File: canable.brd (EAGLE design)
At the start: 19.1 x 45.1 mm, 25 parts, among them J2 USB-MICROB, U2 AP2202K-3.3TRG1, U3 MCP2551

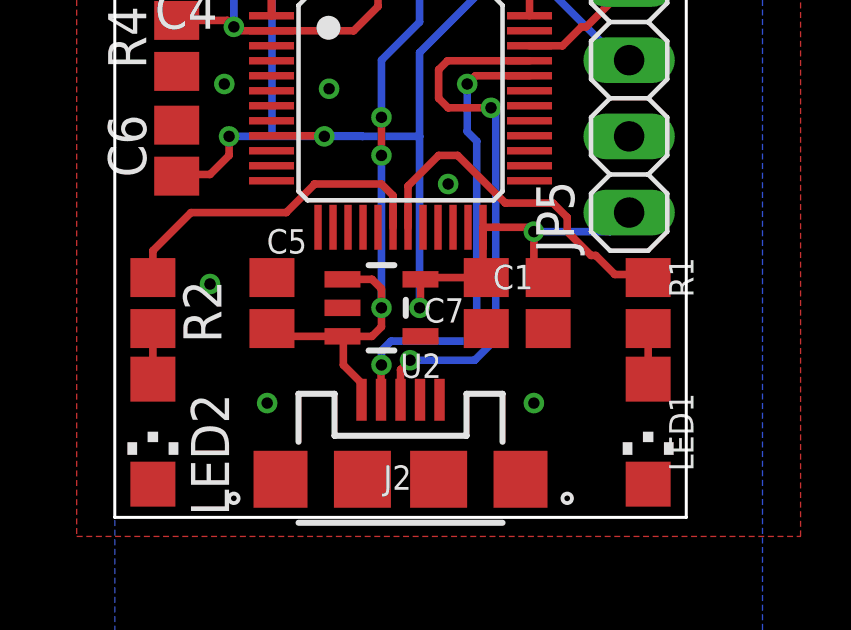
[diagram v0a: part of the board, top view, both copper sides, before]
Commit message: bom changed and screw holes added
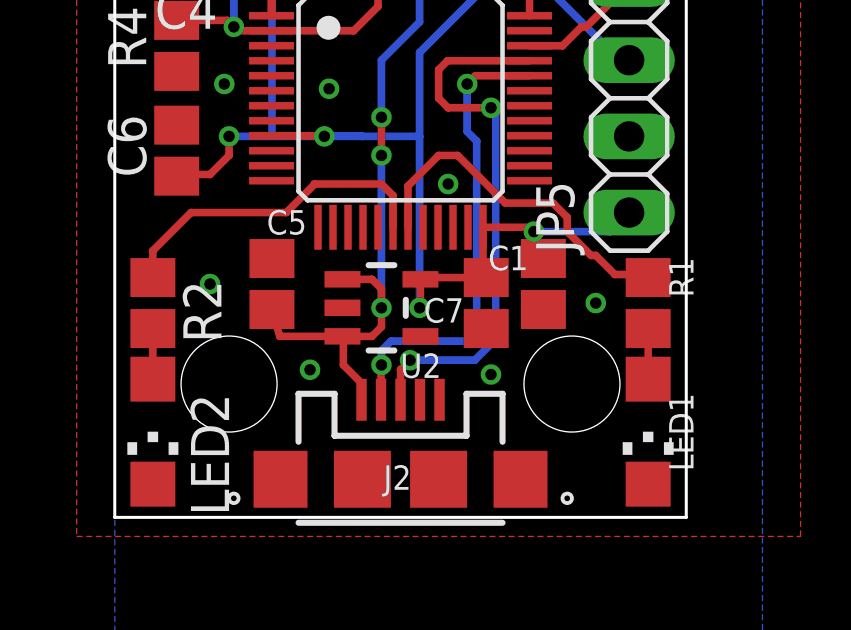
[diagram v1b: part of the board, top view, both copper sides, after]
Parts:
- moved C1 0.65 mm to (14.3, 7.78)
- moved C5 0.63 mm to (5.24, 7.78)
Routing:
- net V_BATT: track 31.3 -> 31.8 mm
- net GND: vias 11 -> 12
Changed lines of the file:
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@@
 <layer number="23" name="tOrigins" color="15" fill="1" visible="yes" active="yes"/>
 <layer number="24" name="bOrigins" color="15" fill="1" visible="yes" active="yes"/>
-<layer number="25" name="tNames" color="7" fill="1" visible="no" active="yes"/>
-<layer number="26" name="bNames" color="7" fill="1" visible="no" active="yes"/>
-<layer number="27" name="tValues" color="7" fill="1" visible="no" active="yes"/>
-<layer number="28" name="bValues" color="7" fill="1" visible="no" active="yes"/>
+<layer number="25" name="tNames" color="7" fill="1" visible="yes" active="yes"/>
+<layer number="26" name="bNames" color="7" fill="1" visible="yes" active="yes"/>
+<layer number="27" name="tValues" color="7" fill="1" visible="yes" active="yes"/>
+<layer number="28" name="bValues" color="7" fill="1" visible="yes" active="yes"/>
 <layer number="29" name="tStop" color="7" fill="3" visible="no" active="yes"/>
 <layer number="30" name="bStop" color="7" fill="6" visible="no" active="yes"/>
@@
 <wire x1="19.05" y1="45.085" x2="19.05" y2="0" width="0.1" layer="20"/>
 <wire x1="19.05" y1="0" x2="0" y2="0" width="0.1" layer="20"/>
+<hole x="3.81" y="4.445" drill="3.2"/>
+<hole x="15.24" y="4.445" drill="3.2"/>
 </plain>
 <attributes>
@@
 <attribute name="VALUE" x="16.7005" y="3.8735" size="0.4064" layer="27" rot="R270"/>
 </element>
-<element name="C5" library="schlager_passiv" package="C0805" value="4.7uF" x="5.23875" y="7.14375" smashed="yes" rot="R270">
-<attribute name="NAME" x="5.064125" y="8.79475" size="0.8128" layer="25" ratio="16"/>
-<attribute name="VALUE" x="4.09575" y="8.22325" size="0.4064" layer="27" rot="R270"/>
+<element name="C5" library="schlager_passiv" package="C0805" value="4.7uF" x="5.23875" y="7.77875" smashed="yes" rot="R270">
+<attribute name="NAME" x="5.064125" y="9.42975" size="0.8128" layer="25" ratio="16"/>
+<attribute name="VALUE" x="4.09575" y="8.85825" size="0.4064" layer="27" rot="R270"/>
 </element>
 <element name="C7" library="schlager_passiv" package="C0805" value="4.7uF" x="12.3825" y="7.14375" smashed="yes" rot="R270">
@@
 <attribute name="VALUE" x="15.748" y="19.08175" size="0.4064" layer="27" rot="R90"/>
 </element>
-<element name="C1" library="schlager_passiv" package="C0805" value="0.1uF" x="14.44625" y="7.14375" smashed="yes" rot="R270">
-<attribute name="NAME" x="12.60475" y="7.604125" size="0.8128" layer="25" ratio="16"/>
-<attribute name="VALUE" x="13.30325" y="8.22325" size="0.4064" layer="27" rot="R270"/>
+<element name="C1" library="schlager_passiv" package="C0805" value="0.1uF" x="14.2875" y="7.77875" smashed="yes" rot="R270">
+<attribute name="NAME" x="12.446" y="8.239125" size="0.8128" layer="25" ratio="16"/>
+<attribute name="VALUE" x="13.1445" y="8.85825" size="0.4064" layer="27" rot="R270"/>
 </element>
 <element name="U3" library="SparkFun-DigitalIC" package="SO08" value="MCP2551" x="9.525" y="23.495">
@@
 <vertex x="-1.27" y="45.085"/>
 </polygon>
-<via x="13.97" y="3.81" extent="1-16" drill="0.381"/>
-<via x="5.08" y="3.81" extent="1-16" drill="0.381"/>
+<via x="16.03375" y="7.14375" extent="1-16" drill="0.381"/>
+<via x="6.50875" y="4.92125" extent="1-16" drill="0.381"/>
 <via x="11.43" y="22.86" extent="1-16" drill="0.381"/>
 <via x="7.14375" y="14.2875" extent="1-16" drill="0.381"/>
@@
 <via x="9.525" y="43.18" extent="1-16" drill="0.381"/>
 <via x="8.09625" y="23.01875" extent="1-16" drill="0.381"/>
+<via x="12.54125" y="4.7625" extent="1-16" drill="0.381"/>
 </signal>
 <signal name="3.3V">
@@
 <contactref element="JP3" pad="1"/>
 <wire x1="13.97" y1="9.525" x2="13.97" y2="8.47" width="0.254" layer="1"/>
-<wire x1="13.97" y1="8.47" x2="14.44625" y2="7.99375" width="0.254" layer="1"/>
+<wire x1="13.97" y1="8.47" x2="14.2875" y2="8.62875" width="0.254" layer="1"/>
 <wire x1="12.275" y1="9.67" x2="12.275" y2="8.10125" width="0.254" layer="1"/>
 <wire x1="12.275" y1="8.10125" x2="12.3825" y2="7.99375" width="0.254" layer="1"/>
@@
 <wire x1="6.19125" y1="23.915" x2="8.7875" y2="23.915" width="0.254" layer="1"/>
 <wire x1="8.7875" y1="23.915" x2="10.16" y2="22.5425" width="0.254" layer="1"/>
-<wire x1="5.4975" y1="6.035" x2="5.23875" y2="6.29375" width="0.254" layer="1"/>
+<wire x1="5.4975" y1="6.035" x2="5.23875" y2="6.92875" width="0.254" layer="1"/>
 </signal>
 <signal name="D+">
